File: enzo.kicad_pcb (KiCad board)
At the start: 2 copper layers, 118 x 95.1 mm, 63 parts, among them SW1 SW_Push, SW10 SW_Push, SW11 SW_Push, SW12 SW_Push, SW13 SW_Push, SW14 SW_Push, SW15 SW_Push, SW16 SW_Push, SW17 locked, SW2 SW_Push, SW3 SW_Push, SW4 SW_Push, SW5 SW_Push, SW6 SW_Push, SW7 SW_Push, SW8 SW_Push, SW9 SW_Push

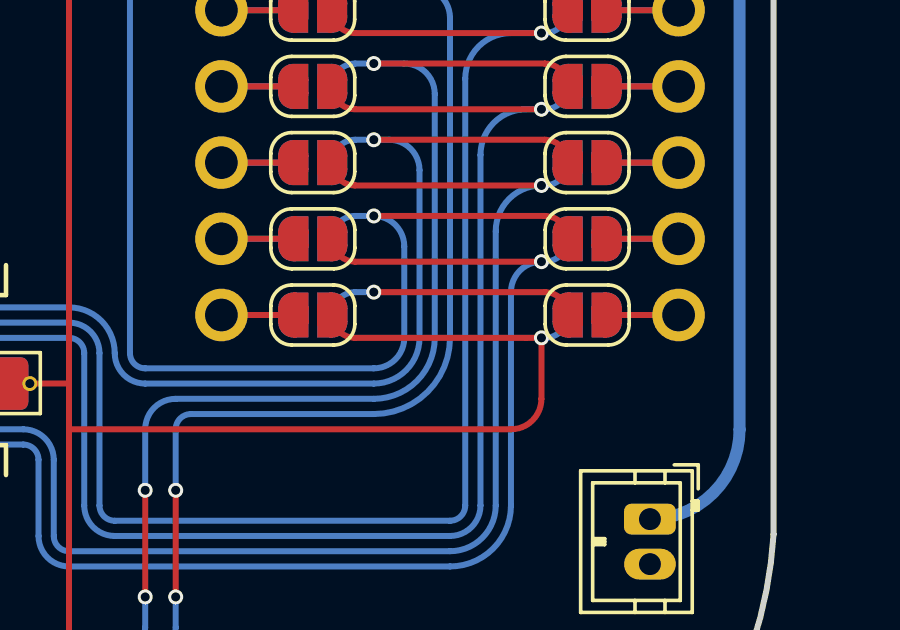
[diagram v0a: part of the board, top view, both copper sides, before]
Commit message: Finally cleaned up jumper situation
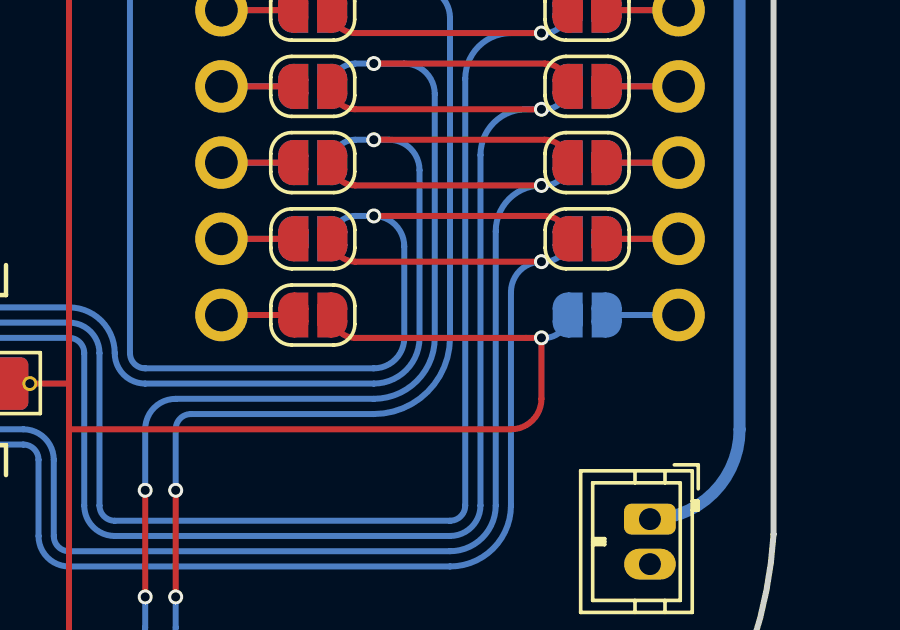
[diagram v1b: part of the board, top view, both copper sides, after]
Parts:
- removed the REF** at (183.4, 94.2)
- removed the REF** at (192.5, 94.2)
- renumbered REF** to JP_col_B1, REF** to JP_col_B2, REF** to JP_col_B3, REF** to JP_col_B4, REF** to JP_col_B5, REF** to JP_col_F1, REF** to JP_col_F2, REF** to JP_col_F3, REF** to JP_col_F4, REF** to JP_col_F5, REF** to JP_row_B1, REF** to JP_row_B2, REF** to JP_row_B3, REF** to JP_row_B4, REF** to JP_row_F1, REF** to JP_row_F2, REF** to JP_row_F3, REF** to JP_row_F4
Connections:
- net Net-(Row5-unused) renamed row5_mcu_unused
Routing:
- net row5_mcu_unused: track 13.4 -> 2.40 mm, vias 1 -> 0
- net col5_mcu: track 4.80 -> 2.40 mm

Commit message: Fix traces
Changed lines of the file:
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@@
   (arc (start 98.552 107.696) (mid 98.91121 107.54721) (end 99.06 107.188) (width 0.2) (layer "F.Cu") (net 22))
   (arc (start 184.032387 84.074) (mid 184.255572 84.612815) (end 184.794387 84.836) (width 0.2) (layer "F.Cu") (net 22))
+  (segment (start 138.684 88.392) (end 138.684 90.932) (width 0.2) (layer "B.Cu") (net 22))
+  (segment (start 158.496 94.488) (end 175.26 94.488) (width 0.2) (layer "B.Cu") (net 22))
+  (segment (start 119.38 92.456) (end 119.38 88.392) (width 0.2) (layer "B.Cu") (net 22))
+  (segment (start 191.008 84.836) (end 191.114387 84.836) (width 0.2) (layer "B.Cu") (net 22))
   (segment (start 176.276 95.504) (end 176.276 100.584) (width 0.2) (layer "B.Cu") (net 22))
-  (segment (start 119.38 92.456) (end 119.38 88.392) (width 0.2) (layer "B.Cu") (net 22))
-  (segment (start 157.48 92.964) (end 157.48 93.98) (width 0.2) (layer "B.Cu") (net 22))
+  (segment (start 188.468 100.584) (end 188.468 86.36) (width 0.2) (layer "B.Cu") (net 22))
+  (segment (start 157.48 92.964) (end 157.48 93.472) (width 0.2) (layer "B.Cu") (net 22))
   (segment (start 101.6 93.472) (end 118.364 93.472) (width 0.2) (layer "B.Cu") (net 22))
-  (segment (start 157.988 94.488) (end 175.26 94.488) (width 0.2) (layer "B.Cu") (net 22))
+  (segment (start 189.992 84.836) (end 191.008 84.836) (width 0.2) (layer "B.Cu") (net 22))
   (segment (start 176.784 101.092) (end 187.96 101.092) (width 0.2) (layer "B.Cu") (net 22))
-  (segment (start 189.992 84.836) (end 191.008 84.836) (width 0.2) (layer "B.Cu") (net 22))
   (segment (start 120.396 87.376) (end 137.668 87.376) (width 0.2) (layer "B.Cu") (net 22))
-  (segment (start 191.008 84.836) (end 191.114387 84.836) (width 0.2) (layer "B.Cu") (net 22))
-  (segment (start 188.468 100.584) (end 188.468 86.36) (width 0.2) (layer "B.Cu") (net 22))
-  (segment (start 138.684 88.392) (end 138.684 90.932) (width 0.2) (layer "B.Cu") (net 22))
   (segment (start 139.7 91.948) (end 156.464 91.948) (width 0.2) (layer "B.Cu") (net 22))
-  (arc (start 156.464 91.948) (mid 157.18242 92.24558) (end 157.48 92.964) (width 0.2) (layer "B.Cu") (net 22))
-  (arc (start 191.114387 84.836) (mid 191.653202 84.612815) (end 191.876387 84.074) (width 0.2) (layer "B.Cu") (net 22))
-  (arc (start 188.468 86.36) (mid 188.914369 85.282369) (end 189.992 84.836) (width 0.2) (layer "B.Cu") (net 22))
-  (arc (start 175.26 94.488) (mid 175.97842 94.78558) (end 176.276 95.504) (width 0.2) (layer "B.Cu") (net 22))
-  (arc (start 119.38 88.392) (mid 119.67758 87.67358) (end 120.396 87.376) (width 0.2) (layer "B.Cu") (net 22))
-  (arc (start 176.276 100.584) (mid 176.42479 100.94321) (end 176.784 101.092) (width 0.2) (layer "B.Cu") (net 22))
+  (arc (start 101.092 93.98) (mid 101.24079 93.62079) (end 101.6 93.472) (width 0.2) (layer "B.Cu") (net 22))
   (arc (start 138.684 90.932) (mid 138.98158 91.65042) (end 139.7 91.948) (width 0.2) (layer "B.Cu") (net 22))
   (arc (start 137.668 87.376) (mid 138.38642 87.67358) (end 138.684 88.392) (width 0.2) (layer "B.Cu") (net 22))
+  (arc (start 119.38 88.392) (mid 119.67758 87.67358) (end 120.396 87.376) (width 0.2) (layer "B.Cu") (net 22))
+  (arc (start 157.48 93.472) (mid 157.77758 94.19042) (end 158.496 94.488) (width 0.2) (layer "B.Cu") (net 22))
+  (arc (start 191.114387 84.836) (mid 191.653202 84.612815) (end 191.876387 84.074) (width 0.2) (layer "B.Cu") (net 22))
+  (arc (start 118.364 93.472) (mid 119.08242 93.17442) (end 119.38 92.456) (width 0.2) (layer "B.Cu") (net 22))
+  (arc (start 156.464 91.948) (mid 157.18242 92.24558) (end 157.48 92.964) (width 0.2) (layer "B.Cu") (net 22))
+  (arc (start 175.26 94.488) (mid 175.97842 94.78558) (end 176.276 95.504) (width 0.2) (layer "B.Cu") (net 22))
   (arc (start 187.96 101.092) (mid 188.31921 100.94321) (end 188.468 100.584) (width 0.2) (layer "B.Cu") (net 22))
-  (arc (start 157.48 93.98) (mid 157.62879 94.33921) (end 157.988 94.488) (width 0.2) (layer "B.Cu") (net 22))
-  (arc (start 101.092 93.98) (mid 101.24079 93.62079) (end 101.6 93.472) (width 0.2) (layer "B.Cu") (net 22))
-  (arc (start 118.364 93.472) (mid 119.08242 93.17442) (end 119.38 92.456) (width 0.2) (layer "B.Cu") (net 22))
+  (arc (start 188.468 86.36) (mid 188.914369 85.282369) (end 189.992 84.836) (width 0.2) (layer "B.Cu") (net 22))
+  (arc (start 176.276 100.584) (mid 176.42479 100.94321) (end 176.784 101.092) (width 0.2) (layer "B.Cu") (net 22))
   (segment (start 117.058 76.708) (end 118.364 76.708) (width 0.2) (layer "F.Cu") (net 23))
   (segment (start 184.796453 87.376) (end 191.008 87.376) (width 0.2) (layer "F.Cu") (net 23))
@@
   (arc (start 184.034453 86.614) (mid 184.257638 87.152815) (end 184.796453 87.376) (width 0.2) (layer "F.Cu") (net 23))
   (arc (start 117.856 95.504) (mid 118.21521 95.35521) (end 118.364 94.996) (width 0.2) (layer "F.Cu") (net 23))
-  (segment (start 157.988 94.996) (end 175.26 94.996) (width 0.2) (layer "B.Cu") (net 23))
+  (segment (start 139.7 92.456) (end 156.464 92.456) (width 0.2) (layer "B.Cu") (net 23))
+  (segment (start 191.116453 87.376) (end 191.008 87.376) (width 0.2) (layer "B.Cu") (net 23))
+  (segment (start 119.888 94.488) (end 119.888 88.392) (width 0.2) (layer "B.Cu") (net 23))
+  (segment (start 158.496 94.996) (end 175.26 94.996) (width 0.2) (layer "B.Cu") (net 23))
+  (segment (start 156.972 92.964) (end 156.972 93.472) (width 0.2) (layer "B.Cu") (net 23))
+  (segment (start 176.784 101.6) (end 187.96 101.6) (width 0.2) (layer "B.Cu") (net 23))
+  (segment (start 188.976 100.584) (end 188.976 88.9) (width 0.2) (layer "B.Cu") (net 23))
   (segment (start 120.396 87.884) (end 137.668 87.884) (width 0.2) (layer "B.Cu") (net 23))
-  (segment (start 156.972 92.964) (end 156.972 93.98) (width 0.2) (layer "B.Cu") (net 23))
-  (segment (start 191.116453 87.376) (end 191.008 87.376) (width 0.2) (layer "B.Cu") (net 23))
+  (segment (start 175.768 95.504) (end 175.768 100.584) (width 0.2) (layer "B.Cu") (net 23))
   (segment (start 190.5 87.376) (end 191.008 87.376) (width 0.2) (layer "B.Cu") (net 23))
-  (segment (start 119.888 94.488) (end 119.888 88.392) (width 0.2) (layer "B.Cu") (net 23))
-  (segment (start 139.7 92.456) (end 156.464 92.456) (width 0.2) (layer "B.Cu") (net 23))
-  (segment (start 175.768 95.504) (end 175.768 100.584) (width 0.2) (layer "B.Cu") (net 23))
-  (segment (start 188.976 100.584) (end 188.976 88.9) (width 0.2) (layer "B.Cu") (net 23))
+  (segment (start 138.176 88.392) (end 138.176 90.932) (width 0.2) (layer "B.Cu") (net 23))
   (segment (start 117.058 95.504) (end 118.872 95.504) (width 0.2) (layer "B.Cu") (net 23))
-  (segment (start 138.176 88.392) (end 138.176 90.932) (width 0.2) (layer "B.Cu") (net 23))
-  (segment (start 176.784 101.6) (end 187.96 101.6) (width 0.2) (layer "B.Cu") (net 23))
   (arc (start 188.976 88.9) (mid 189.422369 87.822369) (end 190.5 87.376) (width 0.2) (layer "B.Cu") (net 23))
   (arc (start 119.888 88.392) (mid 120.03679 88.03279) (end 120.396 87.884) (width 0.2) (layer "B.Cu") (net 23))
+  (arc (start 138.176 90.932) (mid 138.622369 92.009631) (end 139.7 92.456) (width 0.2) (layer "B.Cu") (net 23))
+  (arc (start 187.96 101.6) (mid 188.67842 101.30242) (end 188.976 100.584) (width 0.2) (layer "B.Cu") (net 23))
+  (arc (start 156.972 93.472) (mid 157.418369 94.549631) (end 158.496 94.996) (width 0.2) (layer "B.Cu") (net 23))
+  (arc (start 137.668 87.884) (mid 138.02721 88.03279) (end 138.176 88.392) (width 0.2) (layer "B.Cu") (net 23))
+  (arc (start 191.878453 86.614) (mid 191.655268 87.152815) (end 191.116453 87.376) (width 0.2) (layer "B.Cu") (net 23))
+  (arc (start 118.872 95.504) (mid 119.59042 95.20642) (end 119.888 94.488) (width 0.2) (layer "B.Cu") (net 23))
+  (arc (start 175.768 100.584) (mid 176.06558 101.30242) (end 176.784 101.6) (width 0.2) (layer "B.Cu") (net 23))
+  (arc (start 175.26 94.996) (mid 175.61921 95.14479) (end 175.768 95.504) (width 0.2) (layer "B.Cu") (net 23))
   (arc (start 156.464 92.456) (mid 156.82321 92.60479) (end 156.972 92.964) (width 0.2) (layer "B.Cu") (net 23))
-  (arc (start 175.26 94.996) (mid 175.61921 95.14479) (end 175.768 95.504) (width 0.2) (layer "B.Cu") (net 23))
-  (arc (start 175.768 100.584) (mid 176.06558 101.30242) (end 176.784 101.6) (width 0.2) (layer "B.Cu") (net 23))
-  (arc (start 138.176 90.932) (mid 138.622369 92.009631) (end 139.7 92.456) (width 0.2) (layer "B.Cu") (net 23))
-  (arc (start 156.972 93.98) (mid 157.26958 94.69842) (end 157.988 94.996) (width 0.2) (layer "B.Cu") (net 23))
-  (arc (start 191.878453 86.614) (mid 191.655268 87.152815) (end 191.116453 87.376) (width 0.2) (layer "B.Cu") (net 23))
-  (arc (start 187.96 101.6) (mid 188.67842 101.30242) (end 188.976 100.584) (width 0.2) (layer "B.Cu") (net 23))
-  (arc (start 118.872 95.504) (mid 119.59042 95.20642) (end 119.888 94.488) (width 0.2) (layer "B.Cu") (net 23))
-  (arc (start 137.668 87.884) (mid 138.02721 88.03279) (end 138.176 88.392) (width 0.2) (layer "B.Cu") (net 23))
   (segment (start 137.16 63.2465) (end 137.16 70.612) (width 0.2) (layer "F.Cu") (net 24))
   (segment (start 135.854 89.408) (end 136.652 89.408) (width 0.2) (layer "F.Cu") (net 24))
